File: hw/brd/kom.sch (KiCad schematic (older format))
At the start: 55 parts

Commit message: Added IR leds to schematic using an NPN single transistor
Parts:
- added D? (x3): IR_LD271, symbol LED
- added Q?: BC547, symbol NPN
- added R?: 10, symbol R
- added R?: 1K, symbol R
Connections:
- net labels added: 5V_IR
- net labels removed: 5V_RGB
- wire segments 157 -> 159
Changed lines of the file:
@@
-EESchema Schematic File Version 2  date Mon 18 Jun 2012 10:35:46 PM CEST
+EESchema Schematic File Version 2  date Tue 19 Jun 2012 11:13:47 PM CEST
 LIBS:power
 LIBS:device
@@
 Sheet 1 1
 Title "KomProject Robot"
-Date "18 jun 2012"
+Date "19 jun 2012"
 Rev ""
 Comp "Universidad Carlos III"
@@
 $EndComp
 Text Label 7400 1950 3    58   ~ 0
-5V_RGB
+5V_IR
 Text Label 7500 1950 3    58   ~ 0
 5V_Encoders
@@
 Text Label 10650 5250 1    58   ~ 0
 5V_Encoders
+Text Label 11100 2500 0    58   ~ 0
+ENC_LA
+Text Label 11100 2600 0    58   ~ 0
+ENC_LB
+Text Label 11100 2700 0    58   ~ 0
+ENC_RA
+Text Label 11100 2800 0    58   ~ 0
+ENC_RB
+Text Label 10950 5800 0    58   ~ 0
+ENC_LA
+$Comp
+L OPTO_NPN Q?
+U 1 1 4FD766B5
+P 11650 6000
+F 0 "Q?" H 11800 6050 50  0000 L CNN
+F 1 "PT480F" H 11800 5900 50  0000 L CNN
+	1    11650 6000
+	1    0    0    -1
+$EndComp
+$Comp
+L LED D?
+U 1 1 4FD766BB
+P 11350 6000
+F 0 "D?" H 11350 6100 50  0000 C CNN
+F 1 "IR_LED" H 11350 5900 50  0000 C CNN
+	1    11350 6000
+	0    1    1    0
+$EndComp
+$Comp
+L R R?
+U 1 1 4FD766C1
+P 11350 5550
+F 0 "R?" V 11430 5550 50  0000 C CNN
+F 1 "220" V 11350 5550 50  0000 C CNN
+	1    11350 5550
+	1    0    0    -1
+$EndComp
+$Comp
+L R R?
+U 1 1 4FD766C7
+P 11750 5550
+F 0 "R?" V 11830 5550 50  0000 C CNN
+F 1 "2.2K" V 11750 5550 50  0000 C CNN
+	1    11750 5550
+	1    0    0    -1
+$EndComp
+$Comp
+L GND #PWR?
+U 1 1 4FD766CD
+P 11550 6250
+F 0 "#PWR?" H 11550 6250 30  0001 C CNN
+F 1 "GND" H 11550 6180 30  0001 C CNN
+	1    11550 6250
+	1    0    0    -1
+$EndComp
+Text Label 11550 5250 1    58   ~ 0
+5V_Encoders
+Text Label 11850 5800 0    58   ~ 0
+ENC_LB
+$Comp
+L OPTO_NPN Q?
+U 1 1 4FD766DE
+P 12550 6000
+F 0 "Q?" H 12700 6050 50  0000 L CNN
+F 1 "PT480F" H 12700 5900 50  0000 L CNN
+	1    12550 6000
+	1    0    0    -1
+$EndComp
+$Comp
+L LED D?
+U 1 1 4FD766E4
+P 12250 6000
+F 0 "D?" H 12250 6100 50  0000 C CNN
+F 1 "IR_LED" H 12250 5900 50  0000 C CNN
+	1    12250 6000
+	0    1    1    0
+$EndComp
+$Comp
+L R R?
+U 1 1 4FD766EA
+P 12250 5550
+F 0 "R?" V 12330 5550 50  0000 C CNN
+F 1 "220" V 12250 5550 50  0000 C CNN
+	1    12250 5550
+	1    0    0    -1
+$EndComp
+$Comp
+L R R?
+U 1 1 4FD766F0
+P 12650 5550
+F 0 "R?" V 12730 5550 50  0000 C CNN
+F 1 "2.2K" V 12650 5550 50  0000 C CNN
+	1    12650 5550
+	1    0    0    -1
+$EndComp
+$Comp
+L GND #PWR?
+U 1 1 4FD766F6
+P 12450 6250
+F 0 "#PWR?" H 12450 6250 30  0001 C CNN
+F 1 "GND" H 12450 6180 30  0001 C CNN
+	1    12450 6250
+	1    0    0    -1
+$EndComp
+Text Label 12450 5250 1    58   ~ 0
+5V_Encoders
+Text Label 12750 5800 0    58   ~ 0
+ENC_RA
+$Comp
+L OPTO_NPN Q?
+U 1 1 4FD76707
+P 13450 6000
+F 0 "Q?" H 13600 6050 50  0000 L CNN
+F 1 "PT480F" H 13600 5900 50  0000 L CNN
+	1    13450 6000
+	1    0    0    -1
+$EndComp
+$Comp
+L LED D?
+U 1 1 4FD7670D
+P 13150 6000
+F 0 "D?" H 13150 6100 50  0000 C CNN
+F 1 "IR_LED" H 13150 5900 50  0000 C CNN
+	1    13150 6000
+	0    1    1    0
+$EndComp
+$Comp
+L R R?
+U 1 1 4FD76713
+P 13150 5550
+F 0 "R?" V 13230 5550 50  0000 C CNN
+F 1 "220" V 13150 5550 50  0000 C CNN
+	1    13150 5550
+	1    0    0    -1
+$EndComp
+$Comp
+L R R?
+U 1 1 4FD76719
+P 13550 5550
+F 0 "R?" V 13630 5550 50  0000 C CNN
+F 1 "2.2K" V 13550 5550 50  0000 C CNN
+	1    13550 5550
+	1    0    0    -1
+$EndComp
+$Comp
+L GND #PWR?
+U 1 1 4FD7671F
+P 13350 6250
+F 0 "#PWR?" H 13350 6250 30  0001 C CNN
+F 1 "GND" H 13350 6180 30  0001 C CNN
+	1    13350 6250
+	1    0    0    -1
+$EndComp
+Text Label 13350 5250 1    58   ~ 0
+5V_Encoders
+Text Label 13650 5800 0    58   ~ 0
+ENC_RB
+$Comp
+L LED D?
+U 1 1 4FE0E9A1
+P 13650 2500
+F 0 "D?" H 13650 2600 50  0000 C CNN
+F 1 "IR_LD271" H 13650 2400 50  0000 C CNN
+	1    13650 2500
+	0    1    1    0
+$EndComp
+$Comp
+L LED D?
+U 1 1 4FE0E9C5
+P 13650 2900
+F 0 "D?" H 13650 3000 50  0000 C CNN
+F 1 "IR_LD271" H 13650 2800 50  0000 C CNN
+	1    13650 2900
+	0    1    1    0
+$EndComp
+$Comp
+L LED D?
+U 1 1 4FE0E9CB
+P 13650 3300
+F 0 "D?" H 13650 3400 50  0000 C CNN
+F 1 "IR_LD271" H 13650 3200 50  0000 C CNN
+	1    13650 3300
+	0    1    1    0
+$EndComp
+$Comp
+L R R?
+U 1 1 4FE0E9EA
+P 13650 2050
+F 0 "R?" V 13730 2050 50  0000 C CNN
+F 1 "10" V 13650 2050 50  0000 C CNN
+	1    13650 2050
+	1    0    0    -1
+$EndComp
+Text Label 13650 1700 1    58   ~ 0
+5V_IR
+$Comp
+L NPN Q?
+U 1 1 4FE0EBB5
+P 13550 3700
+F 0 "Q?" H 13550 3550 50  0000 R CNN
+F 1 "BC547" H 13550 3850 50  0000 R CNN
+	1    13550 3700
+	1    0    0    -1
+$EndComp
+$Comp
+L GND #PWR?
+U 1 1 4FE0EBC4
+P 13650 3900
+F 0 "#PWR?" H 13650 3900 30  0001 C CNN
+F 1 "GND" H 13650 3830 30  0001 C CNN
+	1    13650 3900
+	1    0    0    -1
+$EndComp
+$Comp
+L R R?
+U 1 1 4FE0EBD3
+P 13100 3700
+F 0 "R?" V 13180 3700 50  0000 C CNN
+F 1 "1K" V 13100 3700 50  0000 C CNN
+	1    13100 3700
+	0    -1   -1   0
+$EndComp
 Connection ~ 3750 3050
 Connection ~ 3750 2050
@@
 Wire Wire Line
 	11000 3100 11100 3100
-Text Label 11100 2500 0    58   ~ 0
-ENC_LA
-Text Label 11100 2600 0    58   ~ 0
-ENC_LB
-Text Label 11100 2700 0    58   ~ 0
-ENC_RA
-Text Label 11100 2800 0    58   ~ 0
-ENC_RB
-Text Label 10950 5800 0    58   ~ 0
-ENC_LA
-$Comp
-L OPTO_NPN Q?
-U 1 1 4FD766B5
-P 11650 6000
-F 0 "Q?" H 11800 6050 50  0000 L CNN
-F 1 "PT480F" H 11800 5900 50  0000 L CNN
-	1    11650 6000
-	1    0    0    -1
-$EndComp
-$Comp
-L LED D?
-U 1 1 4FD766BB
-P 11350 6000
-F 0 "D?" H 11350 6100 50  0000 C CNN
-F 1 "IR_LED" H 11350 5900 50  0000 C CNN
-	1    11350 6000
-	0    1    1    0
-$EndComp
-$Comp
-L R R?
-U 1 1 4FD766C1
-P 11350 5550
-F 0 "R?" V 11430 5550 50  0000 C CNN
-F 1 "220" V 11350 5550 50  0000 C CNN
-	1    11350 5550
-	1    0    0    -1
-$EndComp
-$Comp
-L R R?
-U 1 1 4FD766C7
-P 11750 5550
-F 0 "R?" V 11830 5550 50  0000 C CNN
-F 1 "2.2K" V 11750 5550 50  0000 C CNN
-	1    11750 5550
-	1    0    0    -1
-$EndComp
-$Comp
-L GND #PWR?
-U 1 1 4FD766CD
-P 11550 6250
-F 0 "#PWR?" H 11550 6250 30  0001 C CNN
-F 1 "GND" H 11550 6180 30  0001 C CNN
-	1    11550 6250
-	1    0    0    -1
-$EndComp
-Text Label 11550 5250 1    58   ~ 0
-5V_Encoders
 Wire Wire Line
 	11350 6200 11750 6200
@@
 Wire Wire Line
 	11750 5800 11850 5800
-Text Label 11850 5800 0    58   ~ 0
-ENC_LB
-$Comp
-L OPTO_NPN Q?
-U 1 1 4FD766DE
-P 12550 6000
-F 0 "Q?" H 12700 6050 50  0000 L CNN
-F 1 "PT480F" H 12700 5900 50  0000 L CNN
-	1    12550 6000
-	1    0    0    -1
-$EndComp
-$Comp
-L LED D?
-U 1 1 4FD766E4
-P 12250 6000
-F 0 "D?" H 12250 6100 50  0000 C CNN
-F 1 "IR_LED" H 12250 5900 50  0000 C CNN
-	1    12250 6000
-	0    1    1    0
-$EndComp
-$Comp
-L R R?
-U 1 1 4FD766EA
-P 12250 5550
-F 0 "R?" V 12330 5550 50  0000 C CNN
-F 1 "220" V 12250 5550 50  0000 C CNN
-	1    12250 5550
-	1    0    0    -1
-$EndComp
-$Comp
-L R R?
-U 1 1 4FD766F0
-P 12650 5550
-F 0 "R?" V 12730 5550 50  0000 C CNN
-F 1 "2.2K" V 12650 5550 50  0000 C CNN
-	1    12650 5550
-	1    0    0    -1
-$EndComp
-$Comp
-L GND #PWR?
-U 1 1 4FD766F6
-P 12450 6250
-F 0 "#PWR?" H 12450 6250 30  0001 C CNN
-F 1 "GND" H 12450 6180 30  0001 C CNN
-	1    12450 6250
-	1    0    0    -1
-$EndComp
-Text Label 12450 5250 1    58   ~ 0
-5V_Encoders
 Wire Wire Line
 	12250 6200 12650 6200
@@
 Wire Wire Line
 	12650 5800 12750 5800
-Text Label 12750 5800 0    58   ~ 0
-ENC_RA
-$Comp
-L OPTO_NPN Q?
-U 1 1 4FD76707
-P 13450 6000
-F 0 "Q?" H 13600 6050 50  0000 L CNN
-F 1 "PT480F" H 13600 5900 50  0000 L CNN
-	1    13450 6000
-	1    0    0    -1
-$EndComp
-$Comp
-L LED D?
-U 1 1 4FD7670D
-P 13150 6000
-F 0 "D?" H 13150 6100 50  0000 C CNN
-F 1 "IR_LED" H 13150 5900 50  0000 C CNN
-	1    13150 6000
-	0    1    1    0
-$EndComp
-$Comp
-L R R?
-U 1 1 4FD76713
-P 13150 5550
-F 0 "R?" V 13230 5550 50  0000 C CNN
-F 1 "220" V 13150 5550 50  0000 C CNN
-	1    13150 5550
-	1    0    0    -1
-$EndComp
-$Comp
-L R R?
-U 1 1 4FD76719
-P 13550 5550
-F 0 "R?" V 13630 5550 50  0000 C CNN
-F 1 "2.2K" V 13550 5550 50  0000 C CNN
-	1    13550 5550
-	1    0    0    -1
-$EndComp
-$Comp
-L GND #PWR?
-U 1 1 4FD7671F
-P 13350 6250
-F 0 "#PWR?" H 13350 6250 30  0001 C CNN
-F 1 "GND" H 13350 6180 30  0001 C CNN
-	1    13350 6250
-	1    0    0    -1
-$EndComp
-Text Label 13350 5250 1    58   ~ 0
-5V_Encoders
 Wire Wire Line
 	13150 6200 13550 6200
@@
 Wire Wire Line
 	13550 5800 13650 5800
-Text Label 13650 5800 0    58   ~ 0
-ENC_RB
+Wire Wire Line
+	13650 1800 13650 1700
+Wire Wire Line
+	12850 3700 12750 3700
+Text Label 12750 3700 2    58   ~ 0
+D5
 $EndSCHEMATC

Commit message: - Changed all the NPN transistors in the schematic for an encapsulated array - Added libraries for RGB and SHARP
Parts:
- removed BC?, Q?: BC547, symbol NPN
- removed R?: 1K, symbol R
- added LED? (x3): LED_ARBG, symbol LED_ARBG
- added U?: ULN2003A, symbol ULN2003A
- gave numbers to parts that had none: 1
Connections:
- net labels added: IR_GND, LED_GND_B, LED_GND_G, LED_GND_R, PWR_GND_1, PWR_GND_2, RST_SIG
- wire segments 159 -> 189
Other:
- note added: "Motor Control and Encoders"
- note added: "Outputs: RGB and IR"
- moved on the sheet: BT?, C?, D?, IC?, IC?A, M?, P?, Q?, R?, U?, U?A

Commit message: Added fixed sensors
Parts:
- added IR?: GP2D120, symbol GP2Y0A21
- added SRV?: SCANNER_SERVO, symbol CONN_3
- added US?: US_R, symbol ULTRASONICMODULE_SDM-IO
- added US?: US_L, symbol ULTRASONICMODULE_SDM-IO
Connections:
- net labels added: IR_SCANN, US_L_SIG, US_R_SIG
- wire segments 189 -> 245
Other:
- note added: "Sensors"
- moved on the sheet: D?, IC?A, LED?, R?, U?

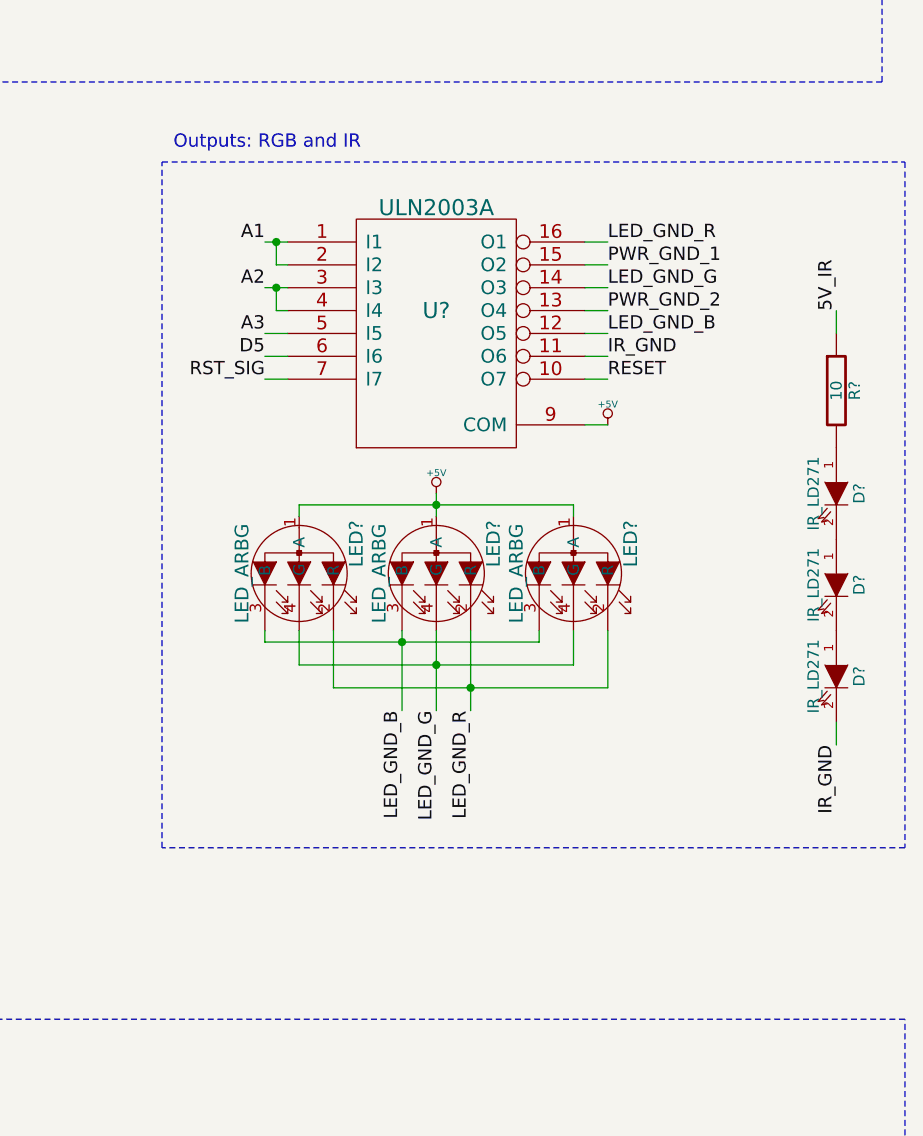
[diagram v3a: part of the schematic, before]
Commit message: Added limiting resistors to RGB leds and changed the one for IR
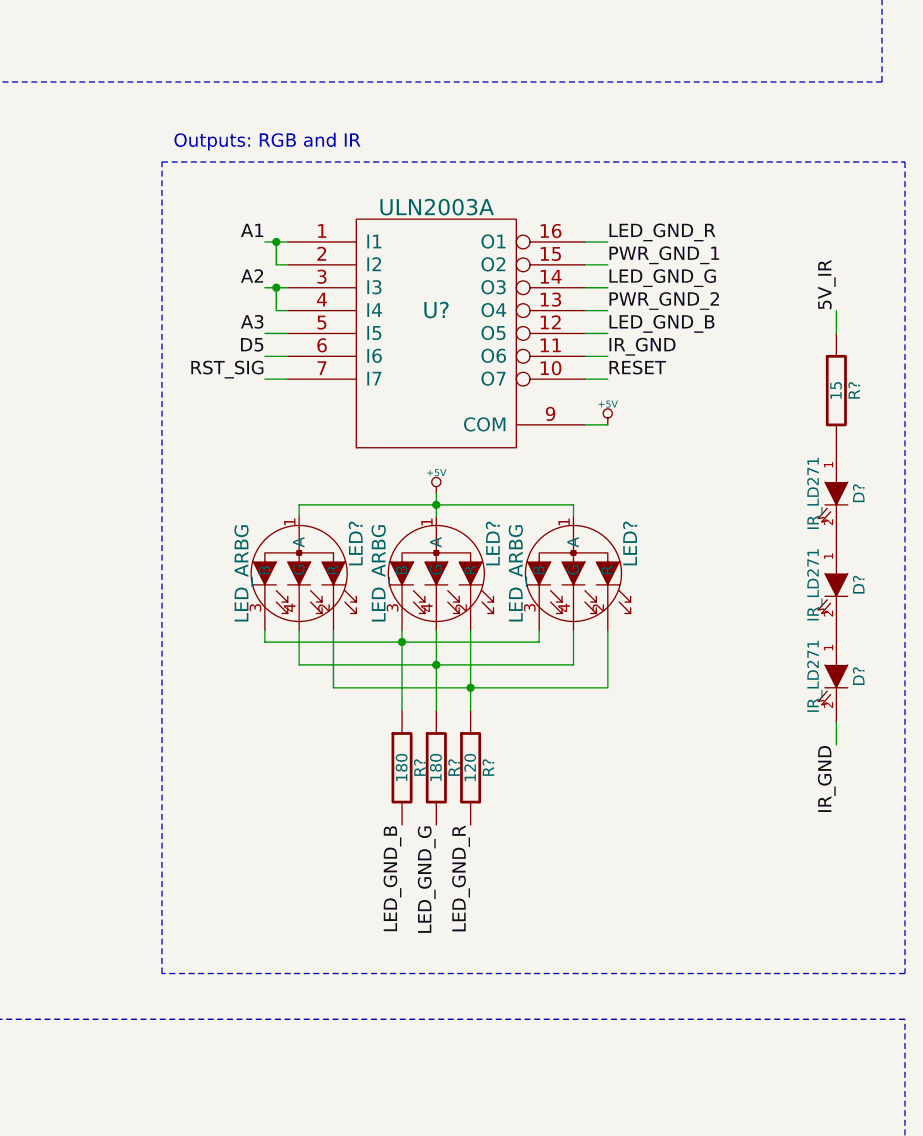
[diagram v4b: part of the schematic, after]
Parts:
- added R? (x2): 180, symbol R
- added R?: 120, symbol R
- R?: value 10 -> 15
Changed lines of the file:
@@
-EESchema Schematic File Version 2  date Wed 20 Jun 2012 12:56:44 AM CEST
+EESchema Schematic File Version 2  date Wed 20 Jun 2012 09:28:04 PM CEST
 LIBS:power
 LIBS:device
@@
 Sheet 1 1
 Title "KomProject Robot"
-Date "19 jun 2012"
+Date "20 jun 2012"
 Rev ""
 Comp "Universidad Carlos III"
@@
 P 15700 5050
 F 0 "R?" V 15780 5050 50  0000 C CNN
-F 1 "10" V 15700 5050 50  0000 C CNN
+F 1 "15" V 15700 5050 50  0000 C CNN
 	1    15700 5050
 	1    0    0    -1
@@
 	1    0    0    -1
 $EndComp
-Text Label 13800 6450 3    58   ~ 0
+Text Label 13800 6950 3    58   ~ 0
 LED_GND_B
-Text Label 13950 6450 3    58   ~ 0
+Text Label 13950 6950 3    58   ~ 0
 LED_GND_G
-Text Label 14100 6450 3    58   ~ 0
+Text Label 14100 6950 3    58   ~ 0
 LED_GND_R
 Text Notes 9250 7750 0    58   ~ 0
@@
 	12750 4050 16000 4050
 Wire Notes Line
-	16000 4050 16000 7050
-Wire Notes Line
-	16000 7050 12750 7050
-Wire Notes Line
-	12750 7050 12750 4050
+	16000 4050 16000 7600
+Wire Notes Line
+	16000 7600 12750 7600
+Wire Notes Line
+	12750 7600 12750 4050
 Wire Wire Line
 	10500 1750 10500 1650
@@
 Text Notes 8250 600  0    58   ~ 0
 Sensors
+$Comp
+L R R?
+U 1 1 4FE22376
+P 13800 6700
+F 0 "R?" V 13880 6700 50  0000 C CNN
+F 1 "180" V 13800 6700 50  0000 C CNN
+	1    13800 6700
+	1    0    0    -1
+$EndComp
+$Comp
+L R R?
+U 1 1 4FE22383
+P 13950 6700
+F 0 "R?" V 14030 6700 50  0000 C CNN
+F 1 "180" V 13950 6700 50  0000 C CNN
+	1    13950 6700
+	1    0    0    -1
+$EndComp
+$Comp
+L R R?
+U 1 1 4FE22389
+P 14100 6700
+F 0 "R?" V 14180 6700 50  0000 C CNN
+F 1 "120" V 14100 6700 50  0000 C CNN
+	1    14100 6700
+	1    0    0    -1
+$EndComp
 $EndSCHEMATC

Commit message: Almost finished with schematic (needs some extra capacitors)
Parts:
- removed IR?: GP2D120, symbol GP2Y0A21
- removed P?: LMotor, symbol CONN_2
- removed P?: RMotor, symbol CONN_2
- removed SRV?: SCANNER_SERVO, symbol CONN_3
- added CP?: PWR1, symbol MOLEX-2
- added CP?: RMotor, symbol MOLEX-2
- added CP?: LMotor, symbol MOLEX-2
- added CP?: PWR2, symbol MOLEX-2
- added D?: DIODE, symbol DIODE
- added JP?: ServoScanner, symbol JP_3
- added P? (x14): GPIO_4PIN, symbol GPIO_4PIN
- added P?: IR_Scanner, symbol GPIO_4PIN
- added R?: 500, symbol R
- added R? (x2): 1.5K, symbol R
- added SW?: TEST, symbol SW_PUSH
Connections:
- net labels added: X0, X1, X2, X3, X4, X5, X6, X7
- wire segments 245 -> 235
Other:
- note added: "50mA"
- note added: "B"
- note added: "Each color of each LED carries 5mA"
- note added: "G"
- note added: "IR"
- note added: "Limiting Resistor"
- note added: "PWM"
- note added: "R"
- moved on the sheet: C?, D?, F?, I2C, LED?, R?, SW?, SW?A, U?, US?

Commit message: Anotated, added some PWRFLAGs, no ERC problems!
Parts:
- gave numbers to parts that had none: 87
- renumbered AREF to AREF1, I2C to I2C1, I2C to I2C2
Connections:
- no-connect marks 1 -> 15
